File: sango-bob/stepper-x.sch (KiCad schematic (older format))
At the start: 26 parts, among them P201 CONN_8, P202 CONN_8, P203 MOT_X, U201 A4985-LP

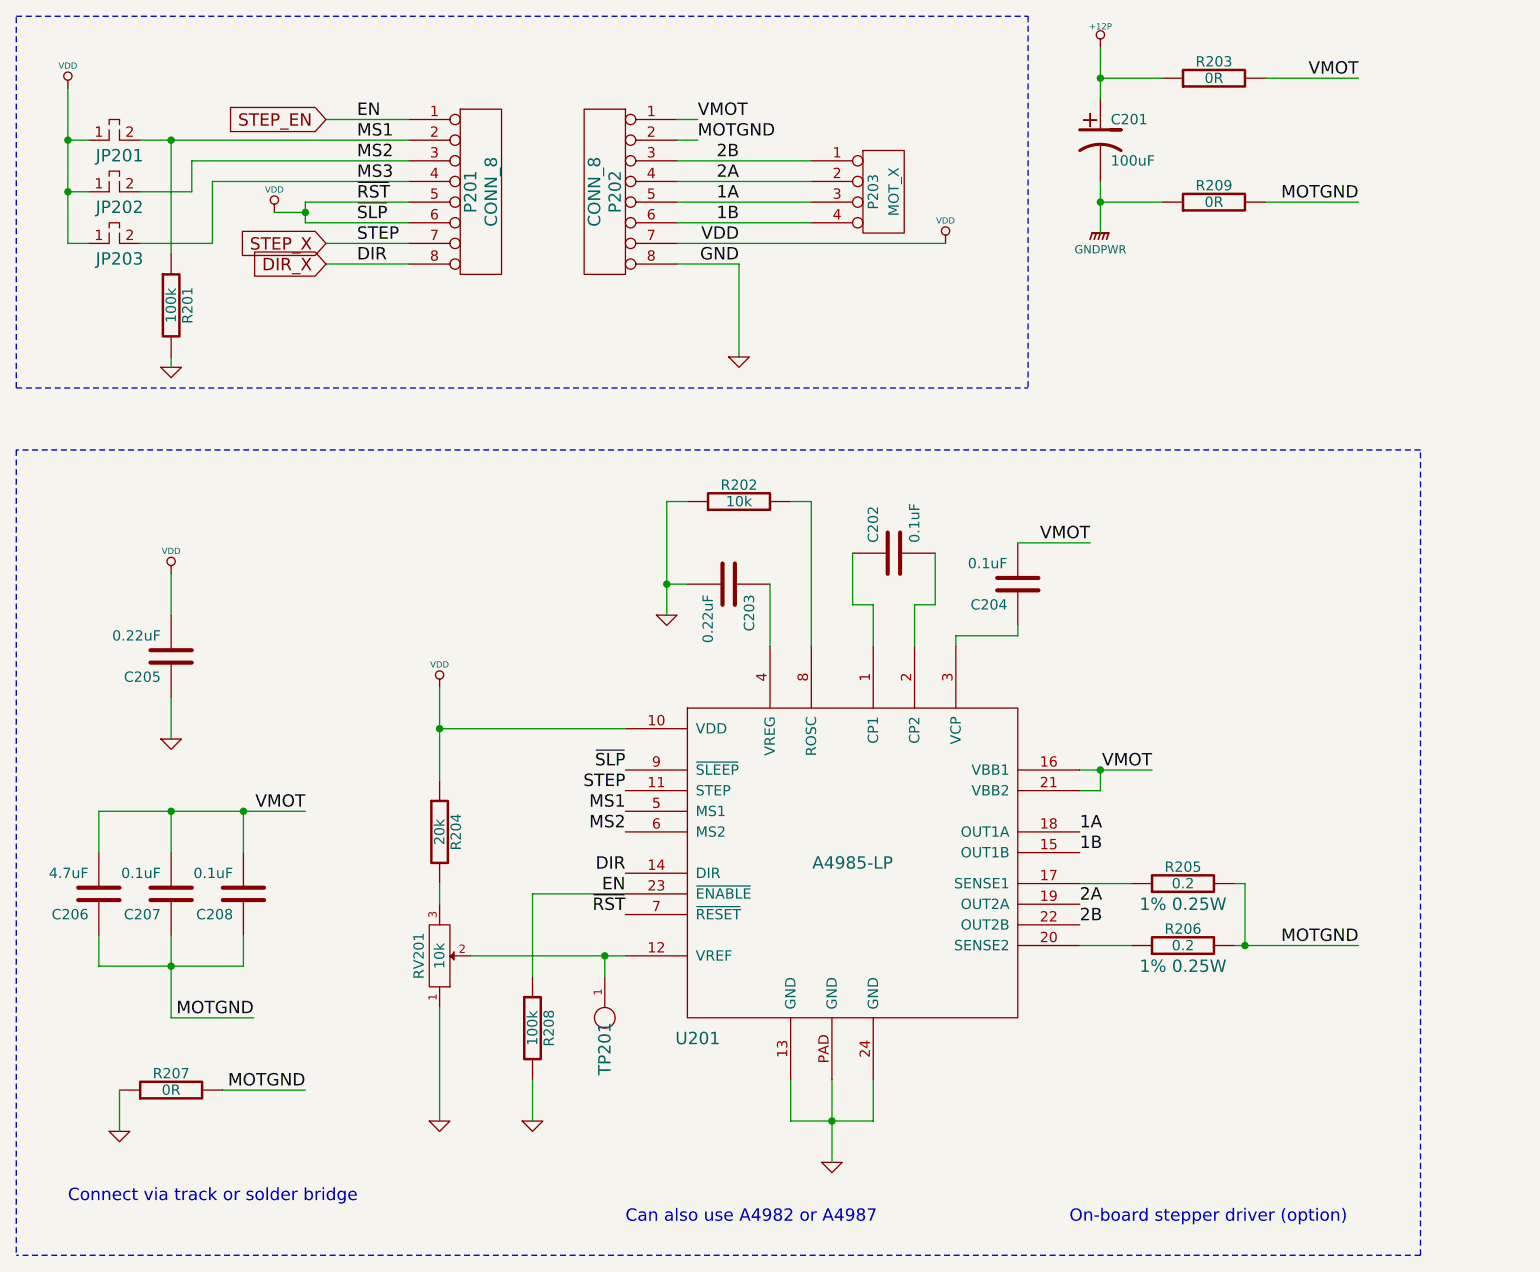
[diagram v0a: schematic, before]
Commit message: Updates to symbols and fix some ERC errors
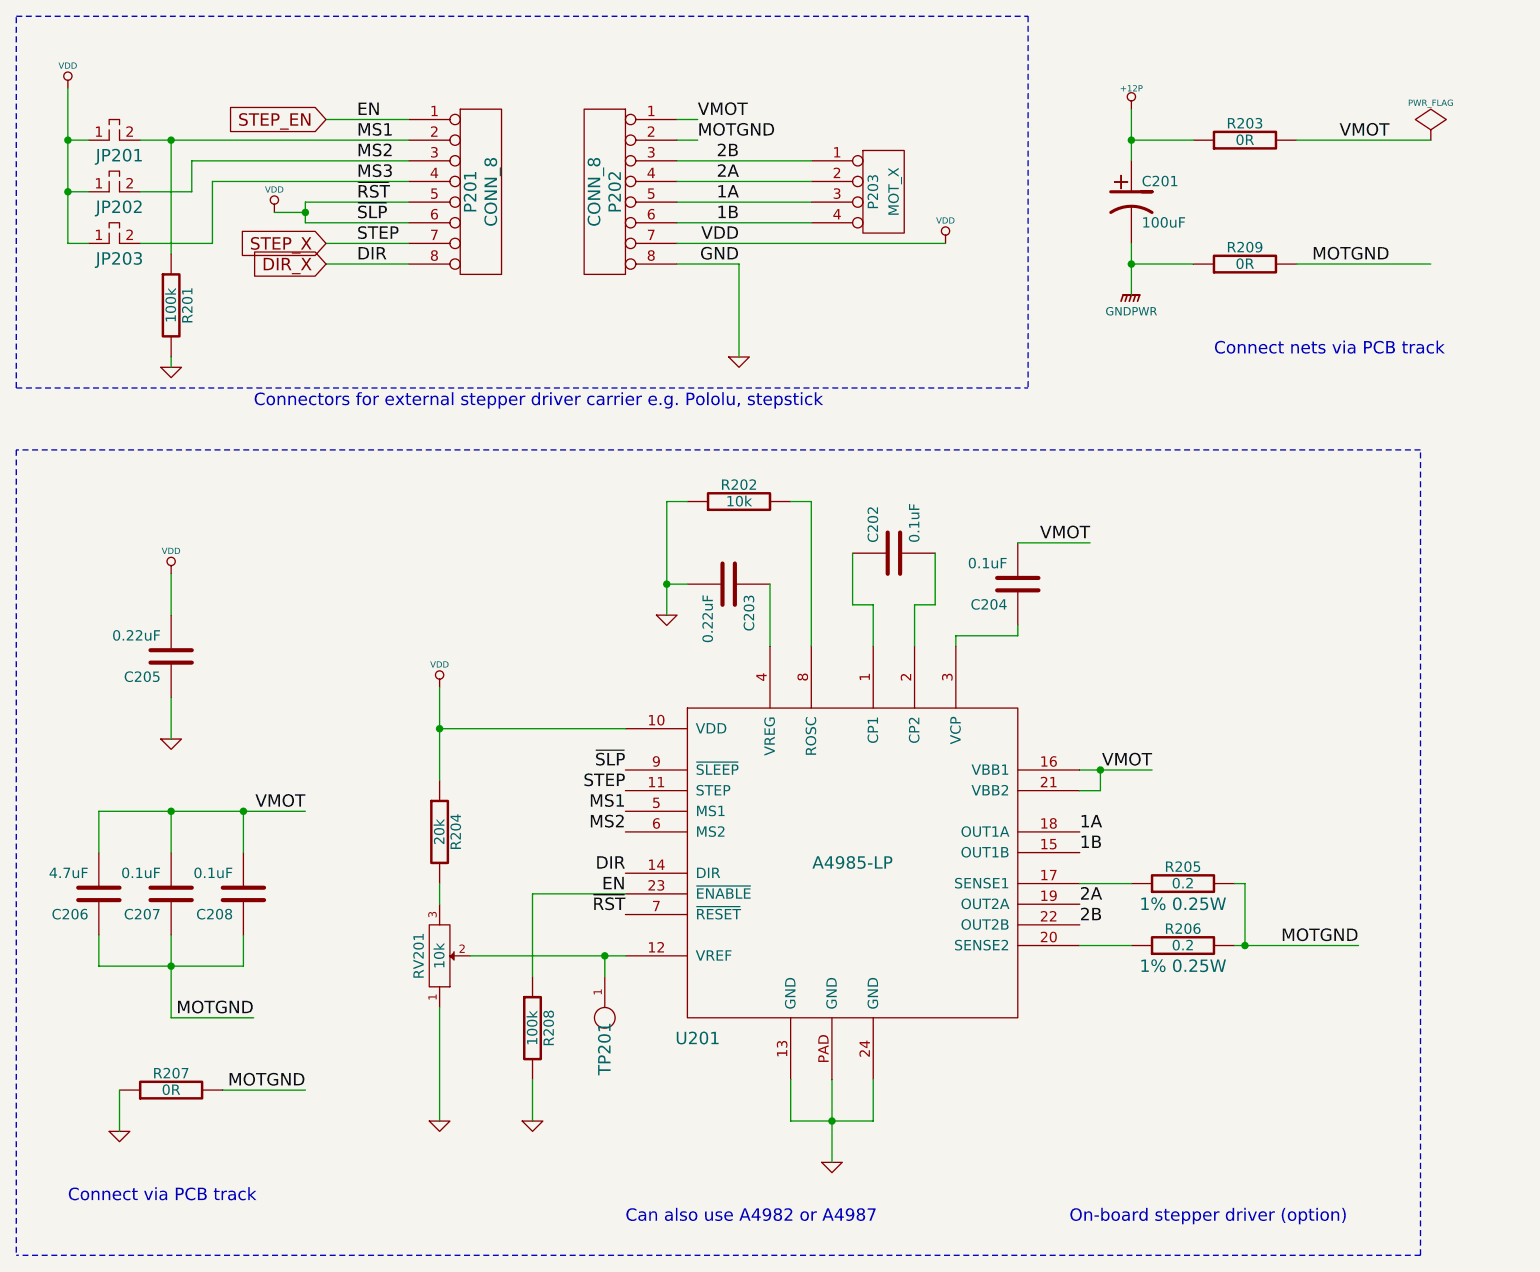
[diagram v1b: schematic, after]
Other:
- note added: "Connect nets via PCB track"
- note added: "Connect via PCB track"
- note added: "Connectors for external stepper driver carrier e.g. Pololu, stepstick"
- note removed: "Connect via track or solder bridge"
- moved on the sheet: C201, R203, R209
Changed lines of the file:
@@
-EESchema Schematic File Version 2  date 03/01/2013 13:12:05
+EESchema Schematic File Version 2  date 22/01/2013 21:21:55
 LIBS:power
 LIBS:device
@@
 Sheet 2 9
 Title ""
-Date "2 jan 2013"
+Date "22 jan 2013"
 Rev ""
 Comp ""
@@
 Comment4 ""
 $EndDescr
-$Comp
-L TEST_POINT_RMC TP201
-U 1 1 50E38145
-P 4900 5400
-F 0 "TP201" H 5100 5400 60  0000 C CNN
-F 1 "TEST_POINT_RMC" H 4900 5550 60  0001 C CNN
-	1    4900 5400
-	0    1    1    0
-$EndComp
+Text Notes 3200 2500 0    60   ~ 0
+Connectors for external stepper driver carrier e.g. Pololu, stepstick
+Text Notes 7850 2250 0    60   ~ 0
+Connect nets via PCB track
+Wire Wire Line
+	8900 1200 8250 1200
 Connection ~ 4900 5150
 Wire Wire Line
@@
 Wire Wire Line
 	5350 1100 5250 1100
-Connection ~ 7300 900
-Wire Wire Line
-	7300 1000 7300 750
+Connection ~ 7450 1200
+Wire Wire Line
+	7450 1300 7450 1050
 Connection ~ 8000 5100
 Wire Wire Line
@@
 Wire Wire Line
 	8000 4800 7950 4800
-Wire Wire Line
-	8550 1500 8100 1500
-Wire Wire Line
-	8550 900  8100 900
 Connection ~ 4100 4050
 Wire Wire Line
@@
 	4100 3850 4100 4300
 Wire Wire Line
-	7600 900  7300 900
-Wire Wire Line
-	7300 1500 7600 1500
+	7750 1200 7450 1200
+Wire Wire Line
+	7450 1800 7750 1800
 Wire Wire Line
 	3050 5800 3450 5800
@@
 	2800 5450 2800 5050
 Wire Wire Line
-	7300 1400 7300 1650
-Connection ~ 7300 1500
+	7450 1700 7450 1950
+Connection ~ 7450 1800
 Wire Wire Line
 	5250 1200 5350 1200
+Wire Wire Line
+	8900 1800 8250 1800
+$Comp
+L PWR_FLAG #FLG01
+U 1 1 50FEFF28
+P 8900 1200
+F 0 "#FLG01" H 8900 1295 30  0001 C CNN
+F 1 "PWR_FLAG" H 8900 1380 30  0000 C CNN
+	1    8900 1200
+	1    0    0    -1
+$EndComp
+$Comp
+L TEST_POINT_RMC TP201
+U 1 1 50E38145
+P 4900 5400
+F 0 "TP201" H 5100 5400 60  0000 C CNN
+F 1 "TEST_POINT_RMC" H 4900 5550 60  0001 C CNN
+	1    4900 5400
+	0    1    1    0
+$EndComp
 Text Label 3200 5450 2    60   ~ 0
 MOTGND
@@
 Text Label 3450 5800 2    60   ~ 0
 MOTGND
-Text Label 8550 1500 2    60   ~ 0
+Text Label 8700 1800 2    60   ~ 0
 MOTGND
 $Comp
 L R R209
 U 1 1 50DEFA2F
-P 7850 1500
-F 0 "R209" V 7930 1500 50  0000 C CNN
-F 1 "0R" V 7850 1500 50  0000 C CNN
-	1    7850 1500
+P 8000 1800
+F 0 "R209" V 8080 1800 50  0000 C CNN
+F 1 "0R" V 8000 1800 50  0000 C CNN
+	1    8000 1800
 	0    -1   -1   0
 $EndComp
-Text Label 8550 900  2    60   ~ 0
+Text Label 8700 1200 2    60   ~ 0
 VMOT
 $Comp
 L R R203
 U 1 1 50E2115B
-P 7850 900
-F 0 "R203" V 7930 900 50  0000 C CNN
-F 1 "0R" V 7850 900 50  0000 C CNN
-	1    7850 900
+P 8000 1200
+F 0 "R203" V 8080 1200 50  0000 C CNN
+F 1 "0R" V 8000 1200 50  0000 C CNN
+	1    8000 1200
 	0    -1   -1   0
 $EndComp
 $Comp
-L VDD #PWR01
+L VDD #PWR02
 U 1 1 50E2115A
 P 2800 3300
-F 0 "#PWR01" H 2800 3400 30  0001 C CNN
+F 0 "#PWR02" H 2800 3400 30  0001 C CNN
 F 1 "VDD" H 2800 3410 30  0000 C CNN
 	1    2800 3300
@@
 $EndComp
 $Comp
-L GND #PWR02
+L GND #PWR03
 U 1 1 50DDCE03
 P 2800 4100
-F 0 "#PWR02" H 2800 4100 30  0001 C CNN
+F 0 "#PWR03" H 2800 4100 30  0001 C CNN
 F 1 "GND" H 2800 4030 30  0001 C CNN
 	1    2800 4100
@@
 $EndComp
 $Comp
-L VDD #PWR03
+L VDD #PWR04
 U 1 1 50DDCD4E
 P 3300 1550
-F 0 "#PWR03" H 3300 1650 30  0001 C CNN
+F 0 "#PWR04" H 3300 1650 30  0001 C CNN
 F 1 "VDD" H 3300 1660 30  0000 C CNN
 	1    3300 1550
@@
 $EndComp
 $Comp
-L GND #PWR04
+L GND #PWR05
 U 1 1 50E21156
 P 6000 6150
-F 0 "#PWR04" H 6000 6150 30  0001 C CNN
+F 0 "#PWR05" H 6000 6150 30  0001 C CNN
 F 1 "GND" H 6000 6080 30  0001 C CNN
 	1    6000 6150
@@
 $EndComp
 $Comp
-L GND #PWR05
+L GND #PWR06
 U 1 1 50D6033D
 P 5200 3500
-F 0 "#PWR05" H 5200 3500 30  0001 C CNN
+F 0 "#PWR06" H 5200 3500 30  0001 C CNN
 F 1 "GND" H 5200 3430 30  0001 C CNN
 	1    5200 3500
@@
 $EndComp
 $Comp
-L GND #PWR06
+L GND #PWR07
 U 1 1 50D6033A
 P 4550 5950
-F 0 "#PWR06" H 4550 5950 30  0001 C CNN
+F 0 "#PWR07" H 4550 5950 30  0001 C CNN
 F 1 "GND" H 4550 5880 30  0001 C CNN
 	1    4550 5950
@@
 $EndComp
 $Comp
-L GND #PWR07
+L GND #PWR08
 U 1 1 50E2114D
 P 4100 5950
-F 0 "#PWR07" H 4100 5950 30  0001 C CNN
+F 0 "#PWR08" H 4100 5950 30  0001 C CNN
 F 1 "GND" H 4100 5880 30  0001 C CNN
 	1    4100 5950
@@
 $EndComp
 $Comp
-L VDD #PWR08
+L VDD #PWR09
 U 1 1 50D60336
 P 4100 3850
-F 0 "#PWR08" H 4100 3950 30  0001 C CNN
+F 0 "#PWR09" H 4100 3950 30  0001 C CNN
 F 1 "VDD" H 4100 3960 30  0000 C CNN
 	1    4100 3850
@@
 $EndComp
 $Comp
-L GND #PWR09
+L GND #PWR010
 U 1 1 50D6032E
 P 2550 6000
-F 0 "#PWR09" H 2550 6000 30  0001 C CNN
+F 0 "#PWR010" H 2550 6000 30  0001 C CNN
 F 1 "GND" H 2550 5930 30  0001 C CNN
 	1    2550 6000
@@
 $EndComp
 Text Notes 2300 6350 0    60   ~ 0
-Connect via track or solder bridge
+Connect via PCB track
 Text Label 5350 1200 0    60   ~ 0
 MOTGND
 $Comp
-L VDD #PWR010
+L VDD #PWR011
 U 1 1 50E21143
 P 6550 1700
-F 0 "#PWR010" H 6550 1800 30  0001 C CNN
+F 0 "#PWR011" H 6550 1800 30  0001 C CNN
 F 1 "VDD" H 6550 1810 30  0000 C CNN
 	1    6550 1700
@@
 $EndComp
 $Comp
-L +12P #PWR011
+L +12P #PWR012
 U 1 1 50D57ED0
-P 7300 750
-F 0 "#PWR011" H 7300 720 30  0001 C CNN
-F 1 "+12P" H 7300 850 30  0000 C CNN
-	1    7300 750
-	1    0    0    -1
-$EndComp
-$Comp
-L VDD #PWR012
+P 7450 1050
+F 0 "#PWR012" H 7450 1020 30  0001 C CNN
+F 1 "+12P" H 7450 1150 30  0000 C CNN
+	1    7450 1050
+	1    0    0    -1
+$EndComp
+$Comp
+L VDD #PWR013
 U 1 1 50E21141
 P 2300 950
-F 0 "#PWR012" H 2300 1050 30  0001 C CNN
+F 0 "#PWR013" H 2300 1050 30  0001 C CNN
 F 1 "VDD" H 2300 1060 30  0000 C CNN
 	1    2300 950
@@
 $EndComp
 $Comp
-L GND #PWR013
+L GND #PWR014
 U 1 1 5071D647
 P 5550 2250
-F 0 "#PWR013" H 5550 2250 30  0001 C CNN
+F 0 "#PWR014" H 5550 2250 30  0001 C CNN
 F 1 "GND" H 5550 2180 30  0001 C CNN
 	1    5550 2250
@@
 $EndComp
 $Comp
-L GND #PWR014
+L GND #PWR015
 U 1 1 5071D642
 P 2800 2300
-F 0 "#PWR014" H 2800 2300 30  0001 C CNN
+F 0 "#PWR015" H 2800 2300 30  0001 C CNN
 F 1 "GND" H 2800 2230 30  0001 C CNN
 	1    2800 2300
@@
 L CP1 C201
 U 1 1 5071D641
-P 7300 1200
-F 0 "C201" H 7350 1300 50  0000 L CNN
-F 1 "100uF" H 7350 1100 50  0000 L CNN
-	1    7300 1200
-	1    0    0    -1
-$EndComp
-$Comp
-L GNDPWR #PWR015
+P 7450 1500
+F 0 "C201" H 7500 1600 50  0000 L CNN
+F 1 "100uF" H 7500 1400 50  0000 L CNN
+	1    7450 1500
+	1    0    0    -1
+$EndComp
+$Comp
+L GNDPWR #PWR016
 U 1 1 5071D63F
-P 7300 1650
-F 0 "#PWR015" H 7300 1700 40  0001 C CNN
-F 1 "GNDPWR" H 7300 1570 40  0000 C CNN
-	1    7300 1650
-	1    0    0    -1
-$EndComp
+P 7450 1950
+F 0 "#PWR016" H 7450 2000 40  0001 C CNN
+F 1 "GNDPWR" H 7450 1870 40  0000 C CNN
+	1    7450 1950
+	1    0    0    -1
+$EndComp
